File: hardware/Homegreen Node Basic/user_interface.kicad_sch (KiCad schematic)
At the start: 21 parts, among them U2 TM1637, U3 FJ3661BH, U4 TTP224

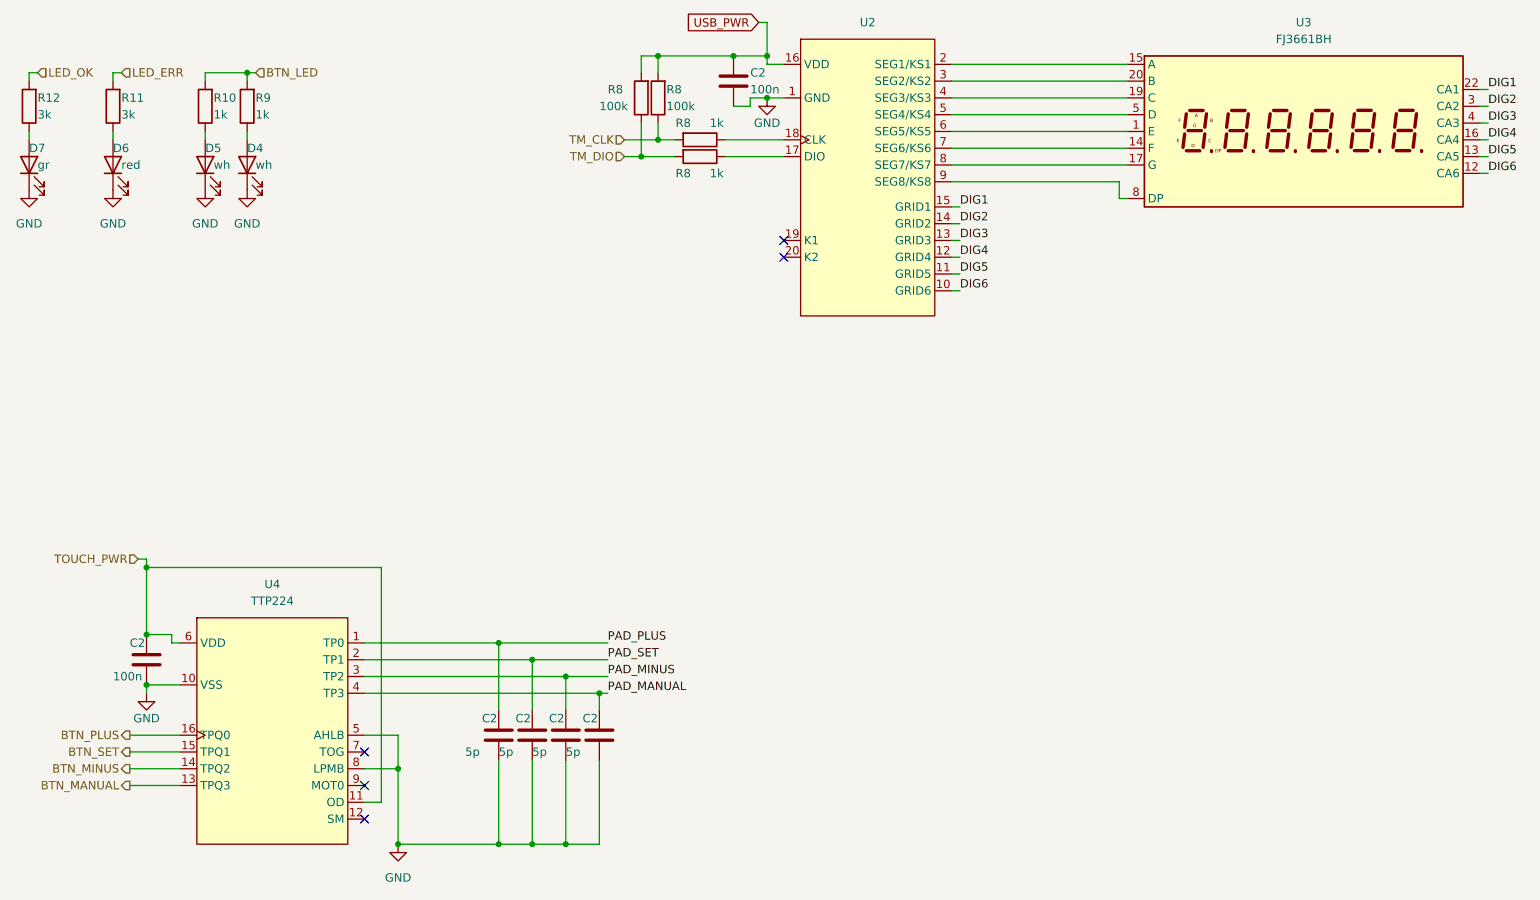
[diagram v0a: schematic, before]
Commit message: - starting with port to atmega328p
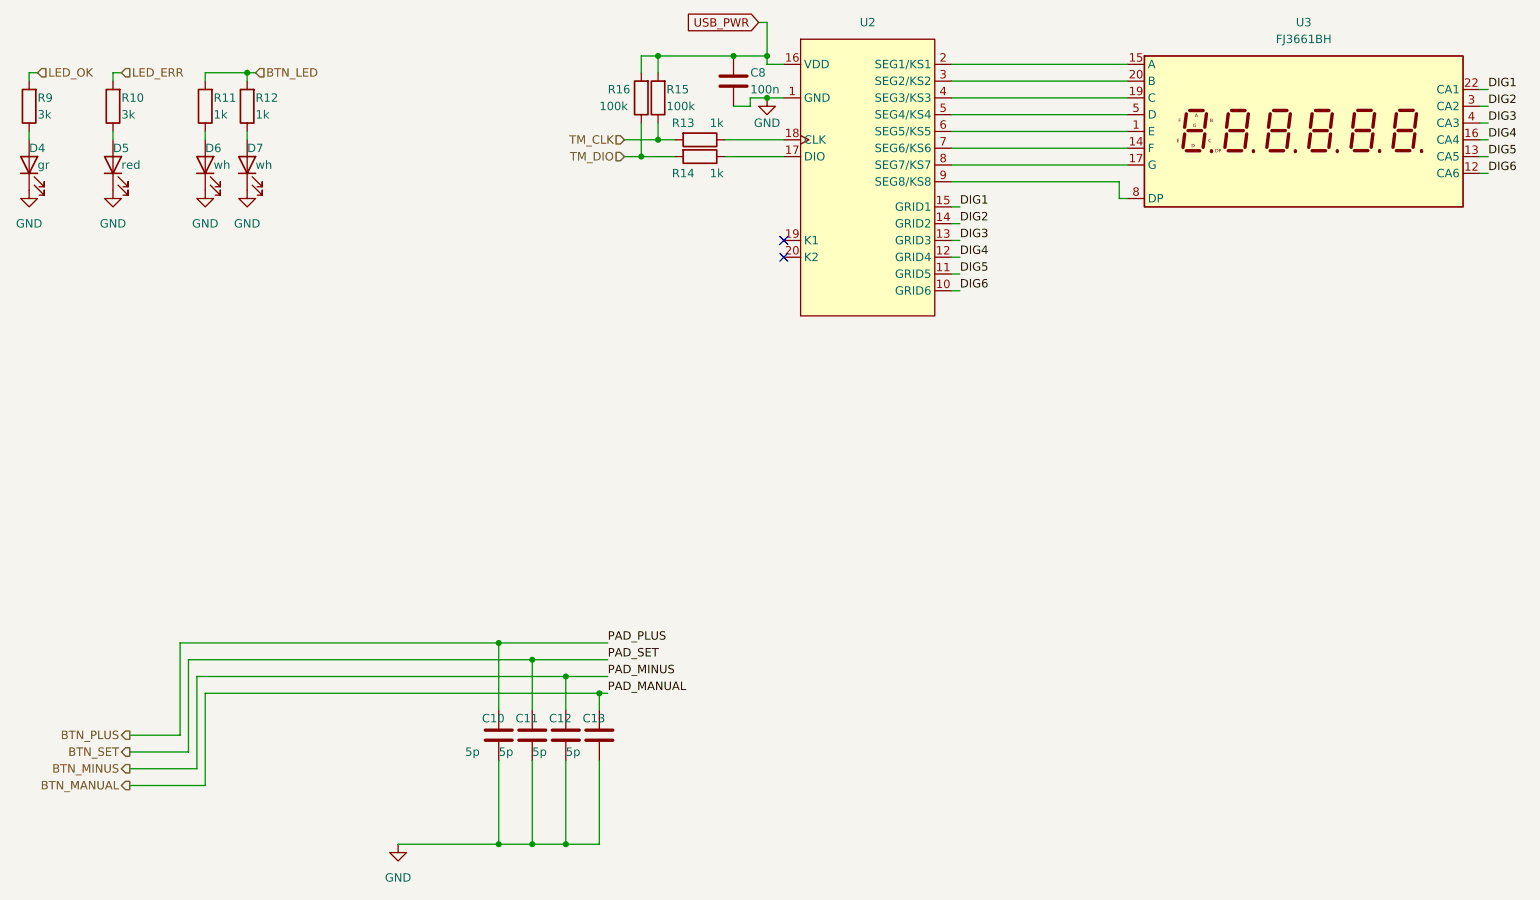
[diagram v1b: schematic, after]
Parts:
- removed C2: 100n, Capacitor_SMD:C_0805_2012Metric, symbol Device:C
- removed U4: TTP224, Package_SO:SSOP-16_3.9x4.9mm_P0.635mm, symbol Pmale_ICs:TTP224
- renumbered C2 to C10, C2 to C11, C2 to C12, C2 to C13, C2 to C8, D7 to D4, D6 to D5, D5 to D6, D4 to D7, R11 to R10, R10 to R11, R9 to R12, R8 to R13, R8 to R14, R8 to R15, R8 to R16, R12 to R9
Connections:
- net PAD_MANUAL is gone; now on net BTN_MANUAL: C13.1
- net PAD_MINUS is gone; now on net BTN_MINUS: C12.1
- net PAD_PLUS is gone; now on net BTN_PLUS: C10.1
- net PAD_SET is gone; now on net BTN_SET: C11.1
- no-connect marks 5 -> 2
